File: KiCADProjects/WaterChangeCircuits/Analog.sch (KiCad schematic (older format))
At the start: 17 parts, among them J57 Conn_01x16, J58 Conn_01x03, J59 Conn_01x03, J60 Conn_01x03, J61 Conn_01x03, J62 Conn_01x03, J63 Conn_01x03, J64 Conn_01x03, J65 Conn_01x03, J66 Conn_01x03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

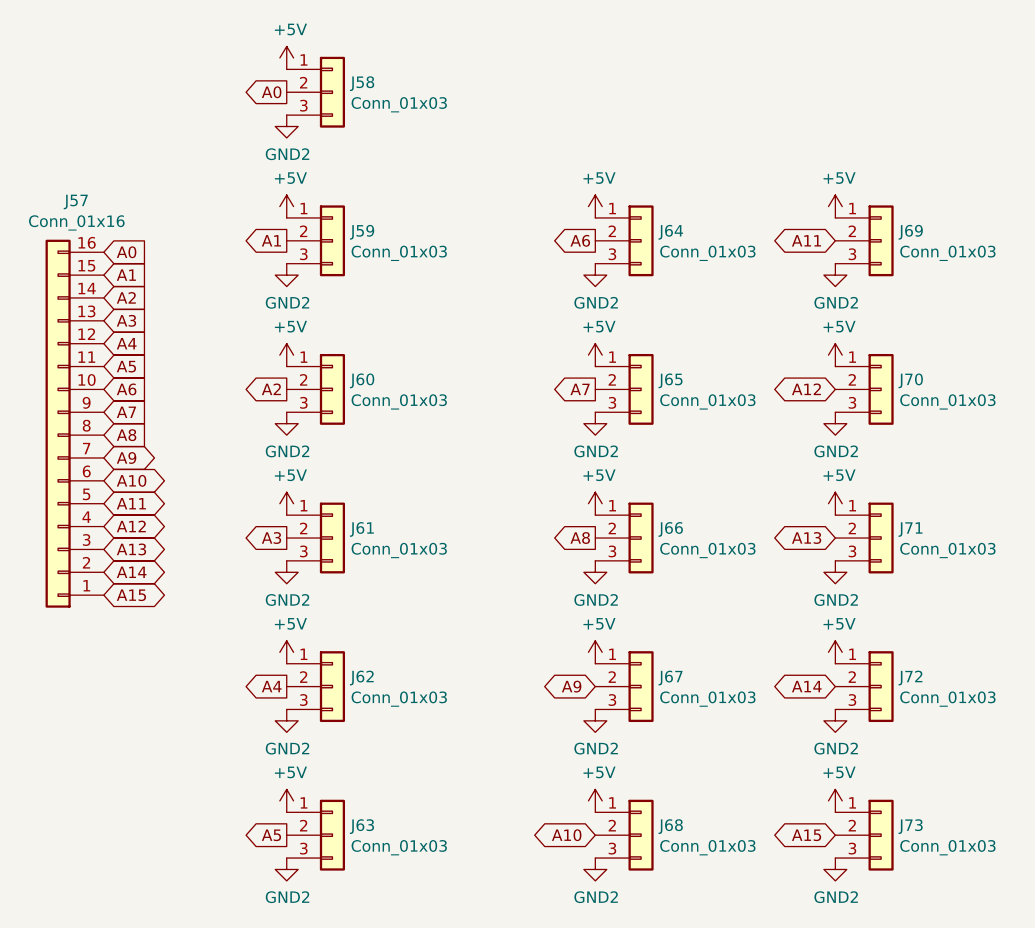
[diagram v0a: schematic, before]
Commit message: Completed PCB design and schematics.
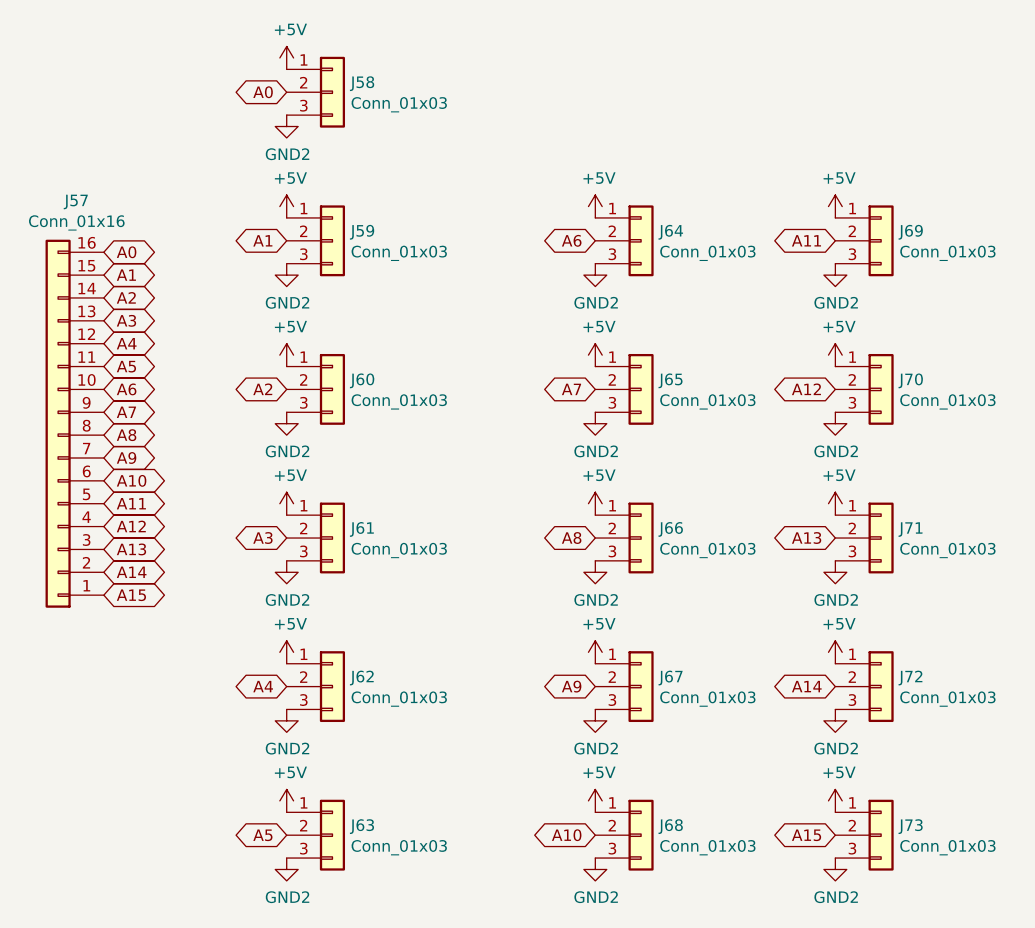
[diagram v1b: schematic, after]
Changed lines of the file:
@@
 	1    0    0    -1
 $EndComp
-Text GLabel 2500 2300 2    50   Input ~ 0
+Text GLabel 2500 2300 2    50   BiDi ~ 0
 A0
-Text GLabel 2500 2400 2    50   Input ~ 0
+Text GLabel 2500 2400 2    50   BiDi ~ 0
 A1
-Text GLabel 2500 2500 2    50   Input ~ 0
+Text GLabel 2500 2500 2    50   BiDi ~ 0
 A2
-Text GLabel 2500 2600 2    50   Input ~ 0
+Text GLabel 2500 2600 2    50   BiDi ~ 0
 A3
-Text GLabel 2500 2700 2    50   Input ~ 0
+Text GLabel 2500 2700 2    50   BiDi ~ 0
 A4
-Text GLabel 2500 2800 2    50   Input ~ 0
+Text GLabel 2500 2800 2    50   BiDi ~ 0
 A5
-Text GLabel 2500 2900 2    50   Input ~ 0
+Text GLabel 2500 2900 2    50   BiDi ~ 0
 A6
-Text GLabel 2500 3000 2    50   Input ~ 0
+Text GLabel 2500 3000 2    50   BiDi ~ 0
 A7
-Text GLabel 2500 3100 2    50   Input ~ 0
+Text GLabel 2500 3100 2    50   BiDi ~ 0
 A8
 Text GLabel 2500 3200 2    50   BiDi ~ 0
@@
 Text GLabel 2500 3800 2    50   BiDi ~ 0
 A15
-Text GLabel 3300 1600 0    50   Output ~ 0
+Text GLabel 3300 1600 0    50   BiDi ~ 0
 A0
-Text GLabel 3300 2250 0    50   Output ~ 0
+Text GLabel 3300 2250 0    50   BiDi ~ 0
 A1
-Text GLabel 3300 2900 0    50   Output ~ 0
+Text GLabel 3300 2900 0    50   BiDi ~ 0
 A2
-Text GLabel 3300 3550 0    50   Output ~ 0
+Text GLabel 3300 3550 0    50   BiDi ~ 0
 A3
-Text GLabel 3300 4200 0    50   Output ~ 0
+Text GLabel 3300 4200 0    50   BiDi ~ 0
 A4
-Text GLabel 3300 4850 0    50   Output ~ 0
+Text GLabel 3300 4850 0    50   BiDi ~ 0
 A5
-Text GLabel 4650 2250 0    50   Output ~ 0
+Text GLabel 4650 2250 0    50   BiDi ~ 0
 A6
-Text GLabel 4650 2900 0    50   Output ~ 0
+Text GLabel 4650 2900 0    50   BiDi ~ 0
 A7
-Text GLabel 4650 3550 0    50   Output ~ 0
+Text GLabel 4650 3550 0    50   BiDi ~ 0
 A8
 Text GLabel 4650 4200 0    50   BiDi ~ 0
